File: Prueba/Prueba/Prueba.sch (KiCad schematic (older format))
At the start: 2 parts, among them U1 dsPIC30F3013

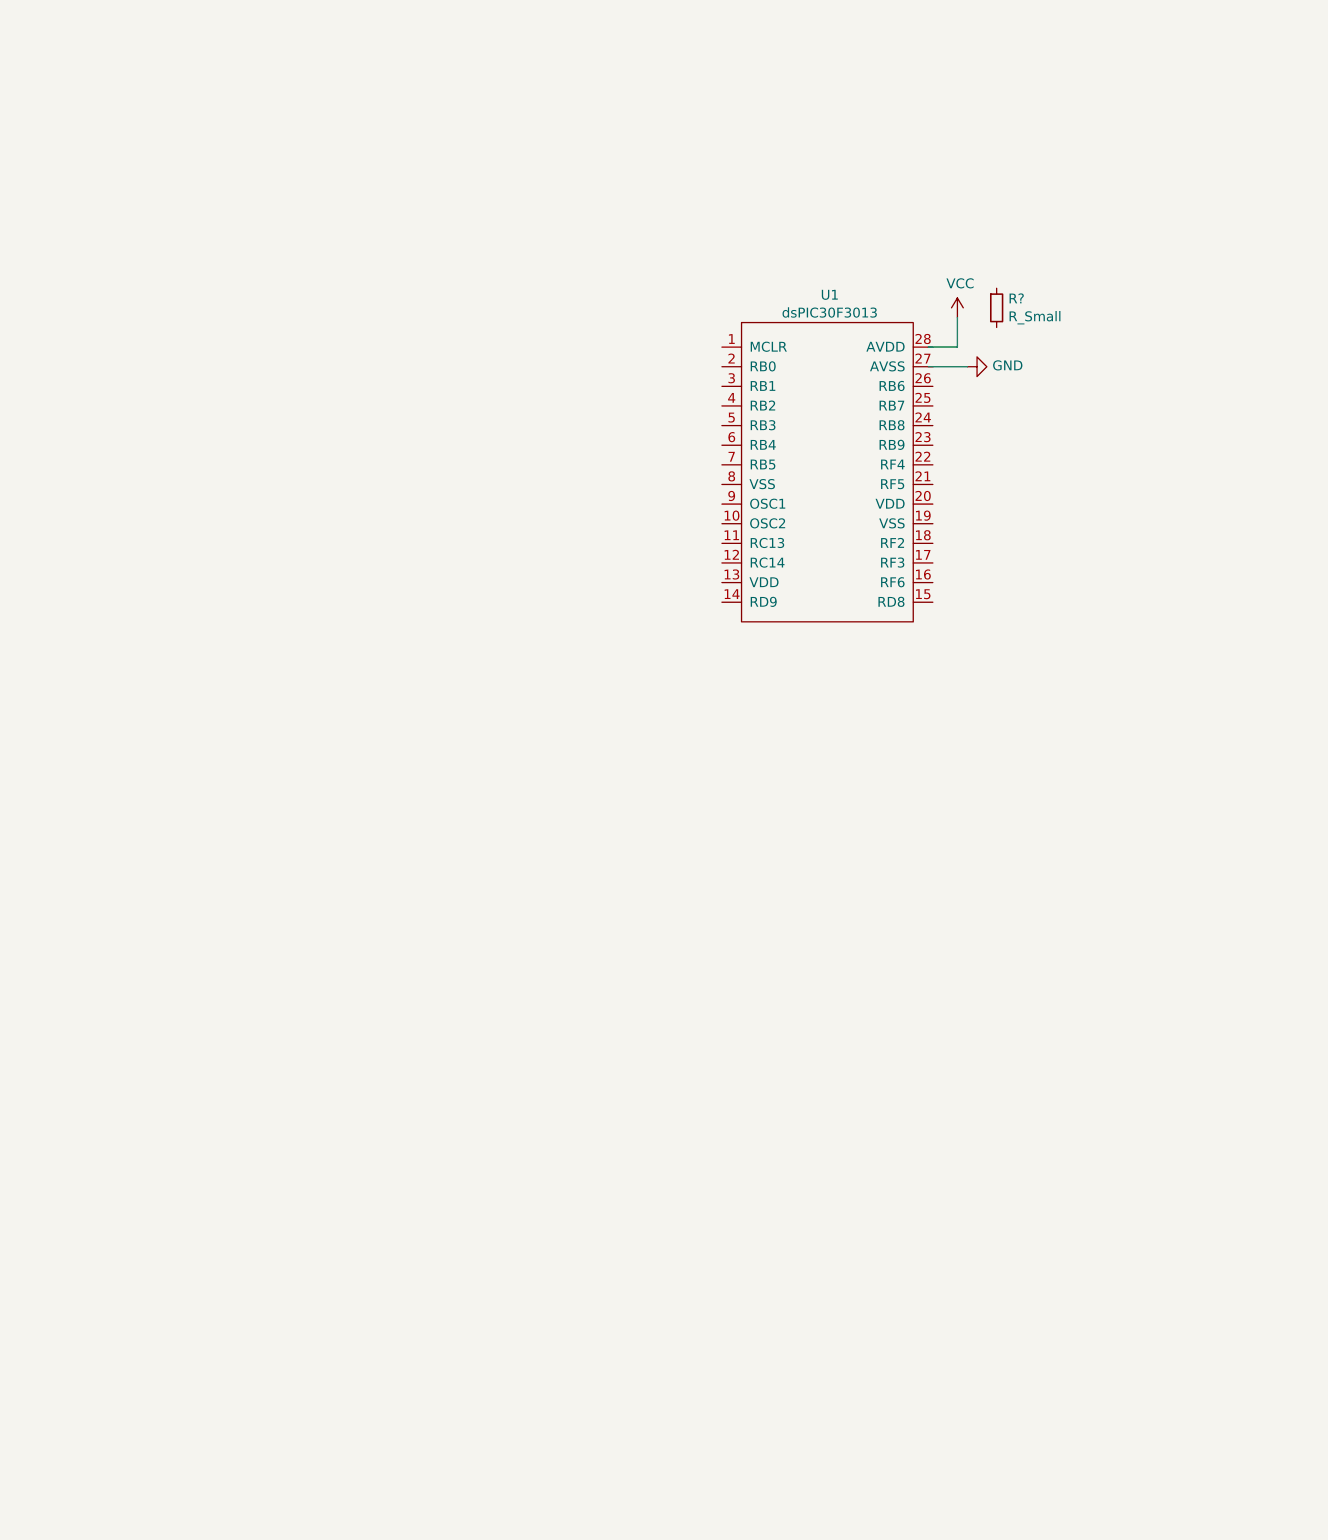
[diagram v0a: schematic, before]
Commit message: Oscilador, reset y caps
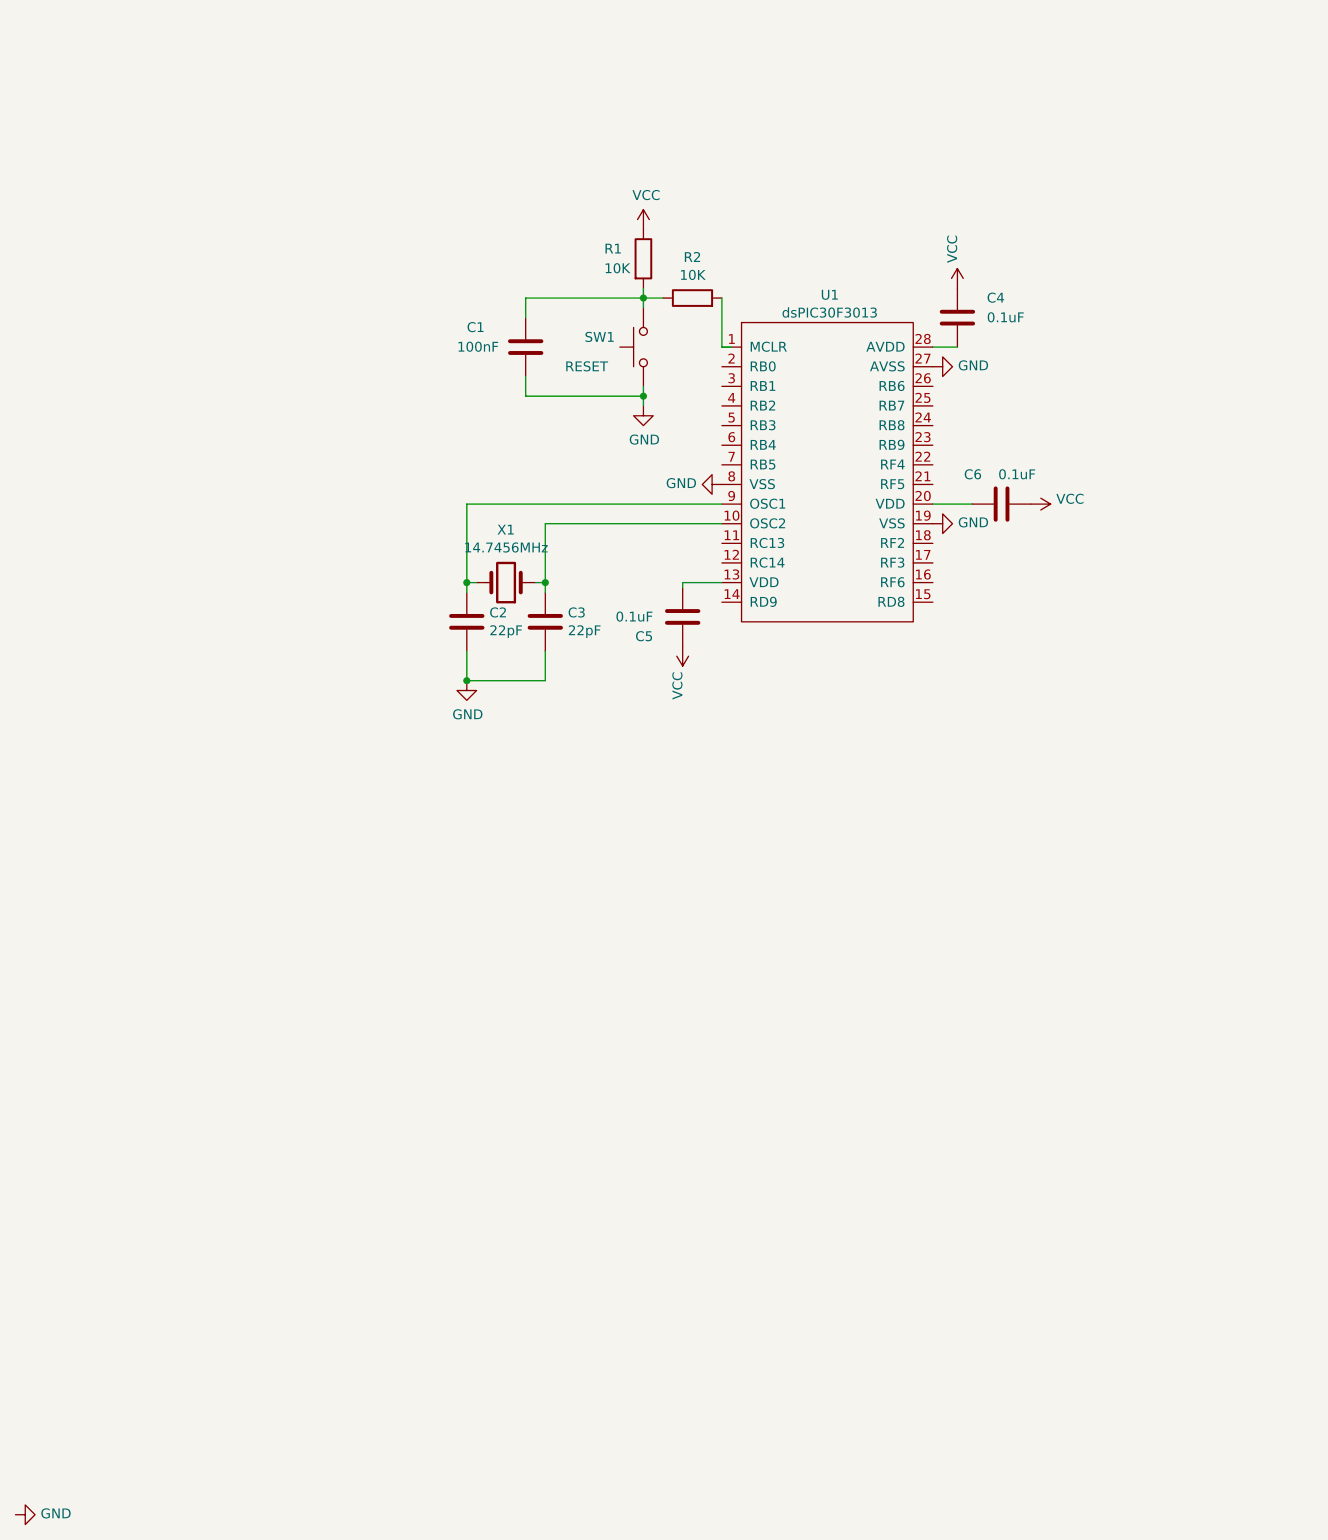
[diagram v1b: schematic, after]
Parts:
- removed R?: R_Small, symbol Device:R_Small
- added C1: 100nF, symbol Device:C
- added C2, C3: 22pF, symbol Device:C
- added C4, C5, C6: 0.1uF, symbol Device:C
- added R1, R2: 10K, symbol Device:R
- added SW1: RESET, symbol Switch:SW_Push
- added X1: 14.7456MHz, symbol Device:Crystal
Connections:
- wire segments 3 -> 26

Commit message: ICSP
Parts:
- removed C4: 0.1uF, symbol Device:C
- added C6: 100nF, symbol Device:C
- added D1: LED, symbol Device:LED
- added J1, J?: Conn_01x11_Male, symbol Connector:Conn_01x11_Male
- added J?: Conn_PIC_ICSP_ICD, symbol Connector:Conn_PIC_ICSP_ICD
- added R3: R, symbol Device:R
- C4: renamed from C6; value 0.1uF -> 100nF
- C5: value 0.1uF -> 100nF
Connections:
- net labels added: OSC2, RB0, RB1, RB2, RB3, RB4, RB5, RB6, RB7, RB8, RB9, RC13, RC14, RD8, RD9, RF2, RF3, RF4, RF5, RF6
- wire segments 26 -> 54
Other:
- moved on the sheet: C4
